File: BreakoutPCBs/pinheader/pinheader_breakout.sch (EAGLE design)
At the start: 2 parts

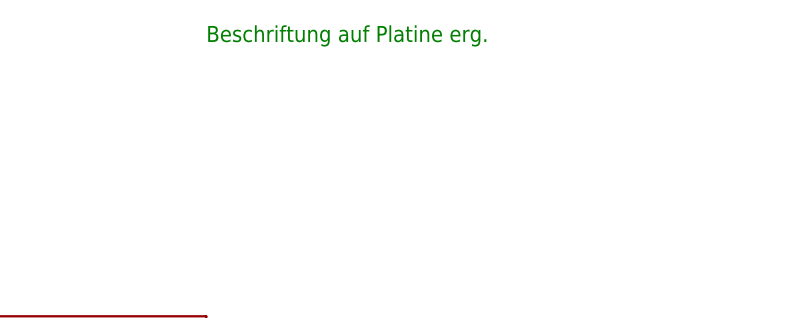
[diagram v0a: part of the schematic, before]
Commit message: update breakout pinheader
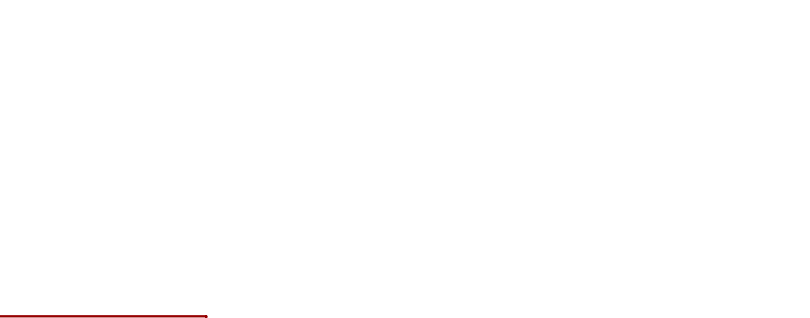
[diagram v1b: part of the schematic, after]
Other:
- note removed: "Beschriftung auf Platine erg."
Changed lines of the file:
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@@
 <sheet>
 <plain>
-<text x="99.06" y="165.1" size="1.778" layer="91">Beschriftung auf Platine erg.</text>
 </plain>
 <instances>
